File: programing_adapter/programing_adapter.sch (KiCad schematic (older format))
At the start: 8 parts, among them J1 Conn_02x05_SWD, J2 USB_A, SW1 SW_RESET

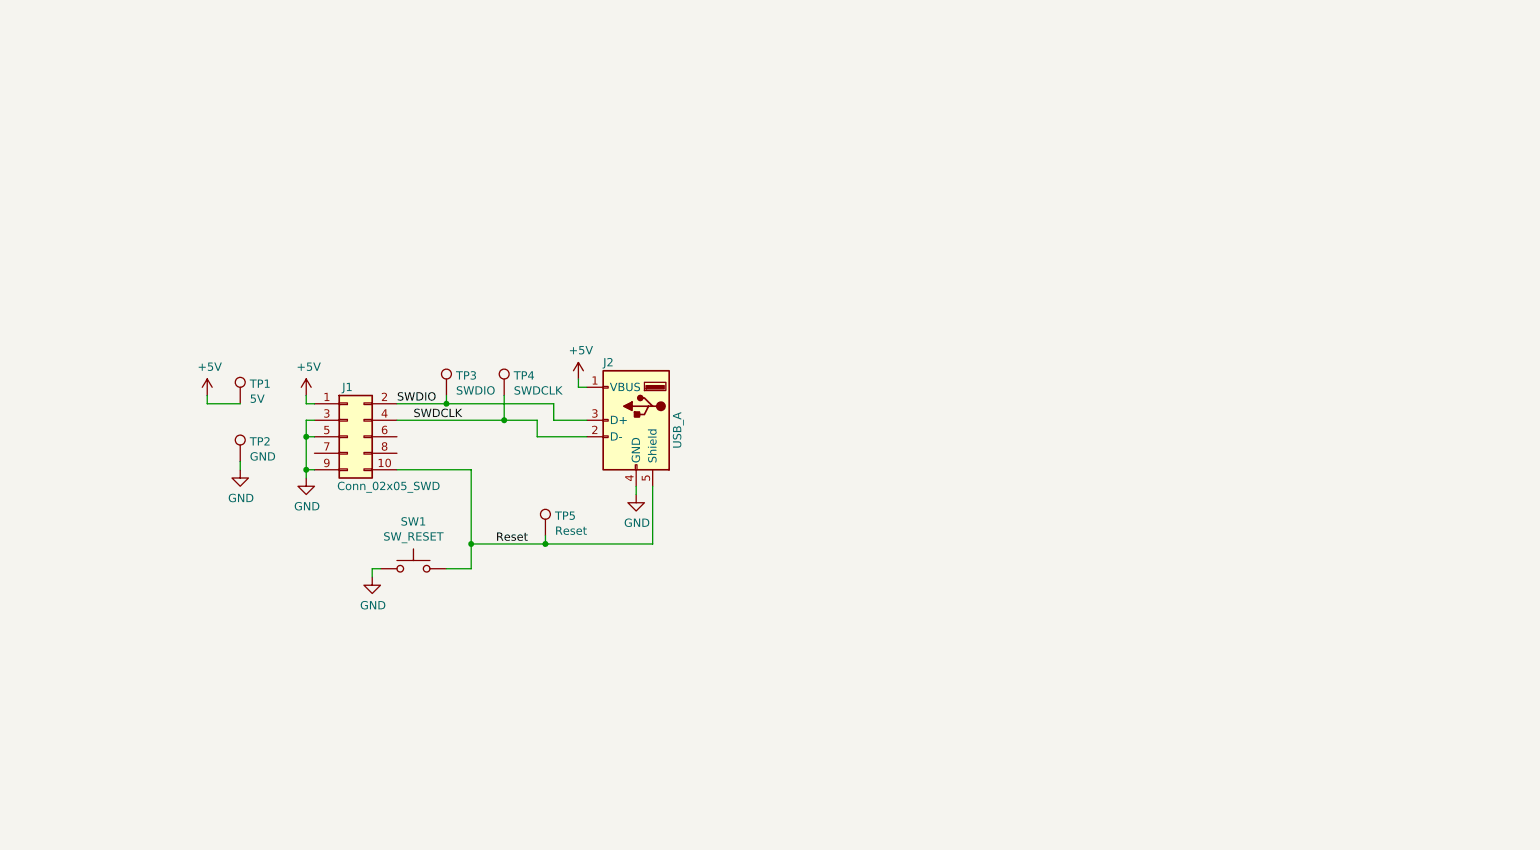
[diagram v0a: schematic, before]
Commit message: remake programming adapter to be much more flexable
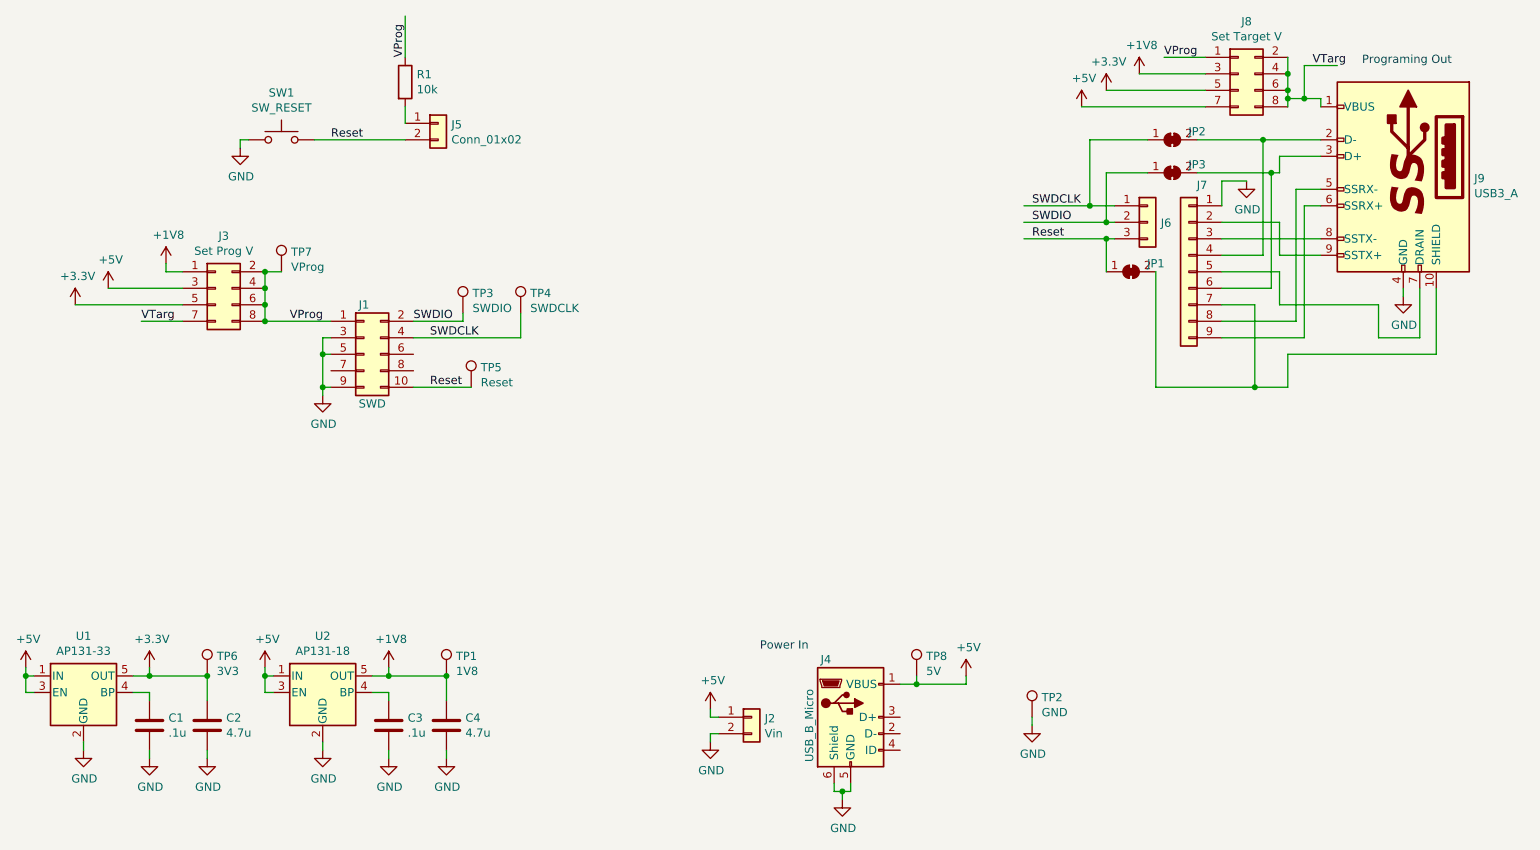
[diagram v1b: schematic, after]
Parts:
- removed J2: USB_A, Connectors:USB_A, symbol Connector:USB_A
- added C1, C3: .1u, Capacitor_SMD:C_0402_1005Metric, symbol Device:C
- added C2, C4: 4.7u, Capacitor_SMD:C_0402_1005Metric, symbol Device:C
- added J2: Vin, Connector_PinHeader_2.54mm:PinHeader_1x02_P2.54mm_Vertical, symbol Connector_Generic:Conn_01x02
- added J3: Set Prog V, Connector_PinHeader_2.54mm:PinHeader_2x04_P2.54mm_Vertical, symbol Connector_Generic:Conn_02x04_Odd_Even
- added J4: USB_B_Micro, Connector_USB:USB_Micro-B_Molex_47346-0001, symbol Connector:USB_B_Micro
- added J5: Conn_01x02, Connector_PinHeader_2.54mm:PinHeader_1x02_P2.54mm_Vertical, symbol Connector_Generic:Conn_01x02
- added J6: Conn_01x03, Connector_PinHeader_2.54mm:PinHeader_1x03_P2.54mm_Vertical, symbol Connector_Generic:Conn_01x03
- added J7: Conn_01x09, Connector_PinHeader_2.54mm:PinHeader_1x09_P2.54mm_Vertical, symbol Connector_Generic:Conn_01x09
- added J8: Set Target V, Connector_PinHeader_2.54mm:PinHeader_2x04_P2.54mm_Vertical, symbol Connector_Generic:Conn_02x04_Odd_Even
- added J9: USB3_A, Connector_USB:USB3_A_Molex_48393-001, symbol Connector:USB3_A
- added JP1, JP2, JP3: SolderJumper_2_Bridged, Jumper:SolderJumper-2_P1.3mm_Bridged_RoundedPad1.0x1.5mm, symbol Jumper:SolderJumper_2_Bridged
- added R1: 10k, Resistor_SMD:R_0402_1005Metric, symbol Device:R
- added TP6: 3V3, TestPoint:TestPoint_Pad_D1.5mm, symbol Connector:TestPoint
- added TP7: VProg, TestPoint:TestPoint_Pad_D1.5mm, symbol Connector:TestPoint
- added TP8: 5V, TestPoint:TestPoint_Pad_D1.5mm, symbol Connector:TestPoint
- added U1: AP131-33, Package_TO_SOT_SMD:SOT-23-5, symbol Regulator_Linear:AP131-33
- added U2: AP131-18, Package_TO_SOT_SMD:SOT-23-5, symbol Regulator_Linear:AP131-18
- J1: value Conn_02x05_SWD -> SWD
- TP1: value 5V -> 1V8; footprint CustomKiCadLibrary:TP_080X080R -> TestPoint:TestPoint_Pad_D1.5mm
- TP2, TP3, TP4, TP5: footprint CustomKiCadLibrary:TP_080X080R -> TestPoint:TestPoint_Pad_D1.5mm
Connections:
- net labels added: +1V8, +3.3V, VProg, VTarg
- wire segments 34 -> 127
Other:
- note added: "Power In"
- note added: "Programing Out"
- moved on the sheet: J1, SW1, TP1, TP2, TP3, TP4, TP5
